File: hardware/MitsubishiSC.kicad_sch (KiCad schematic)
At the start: 68 parts, among them J1 CN105, J2 USB_C_Receptacle_USB2.0_16P, Q1 BSS138, Q2 BSS138, SW3 SPST, SW4 SPST, U1 TPS562203, U3 ESP32-C3-WROOM-02, U4 USBLC6-2SC6, U5 TLV75733PDBV

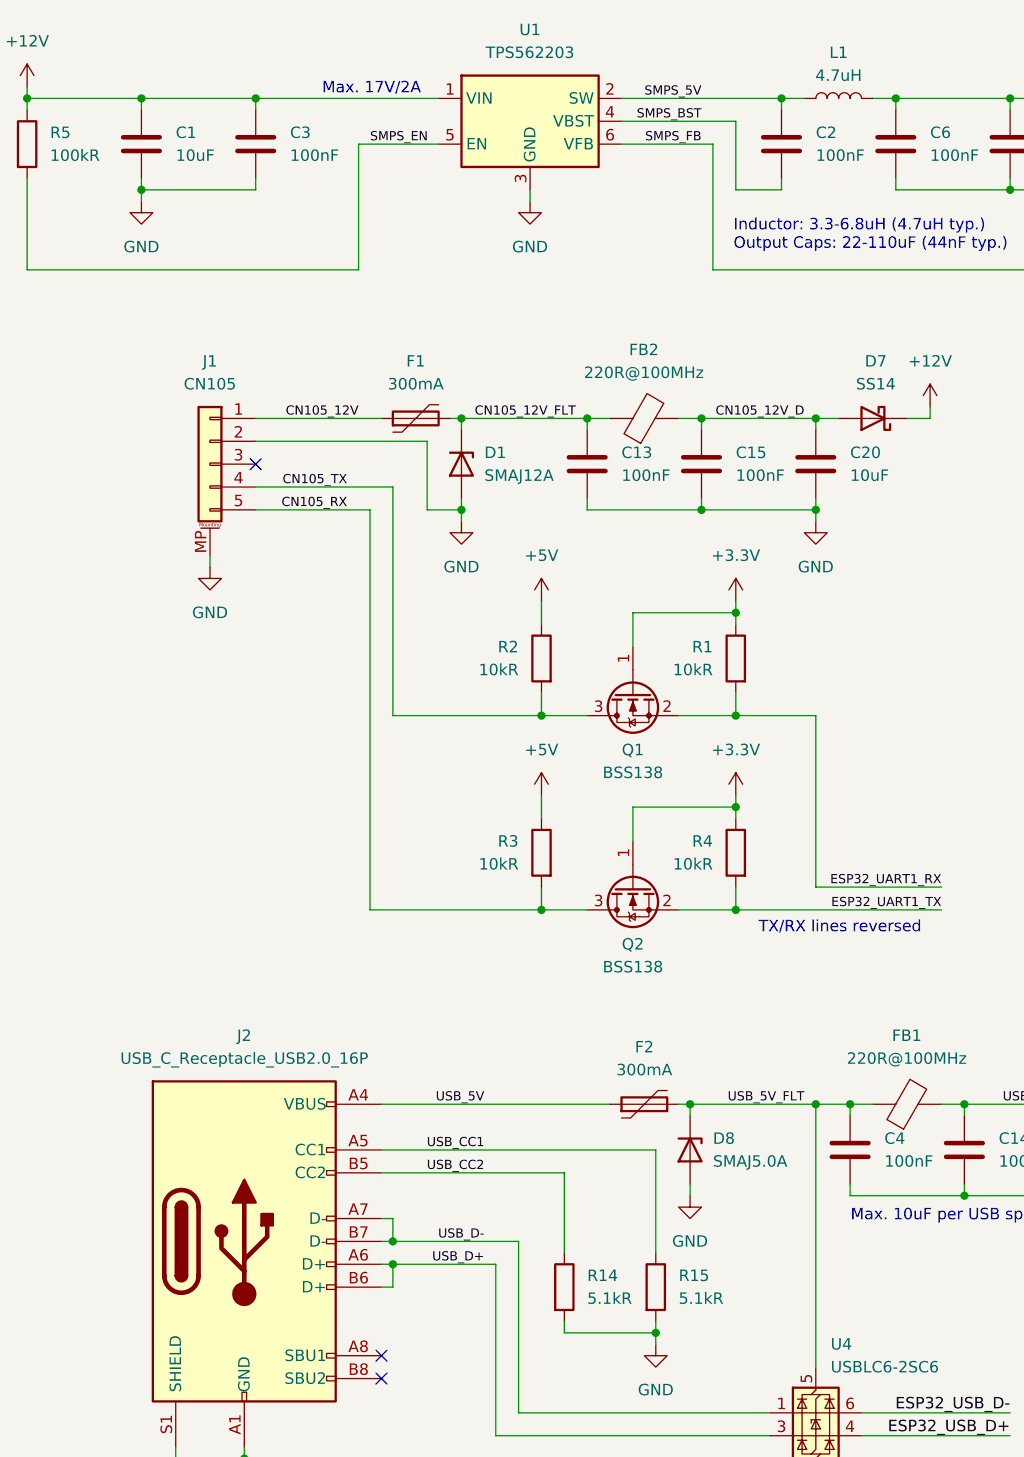
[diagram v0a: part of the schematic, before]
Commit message: feat: upgrade to KiCad v9 (#14)
This commit upgrades the KiCad files to `9.0.4`.
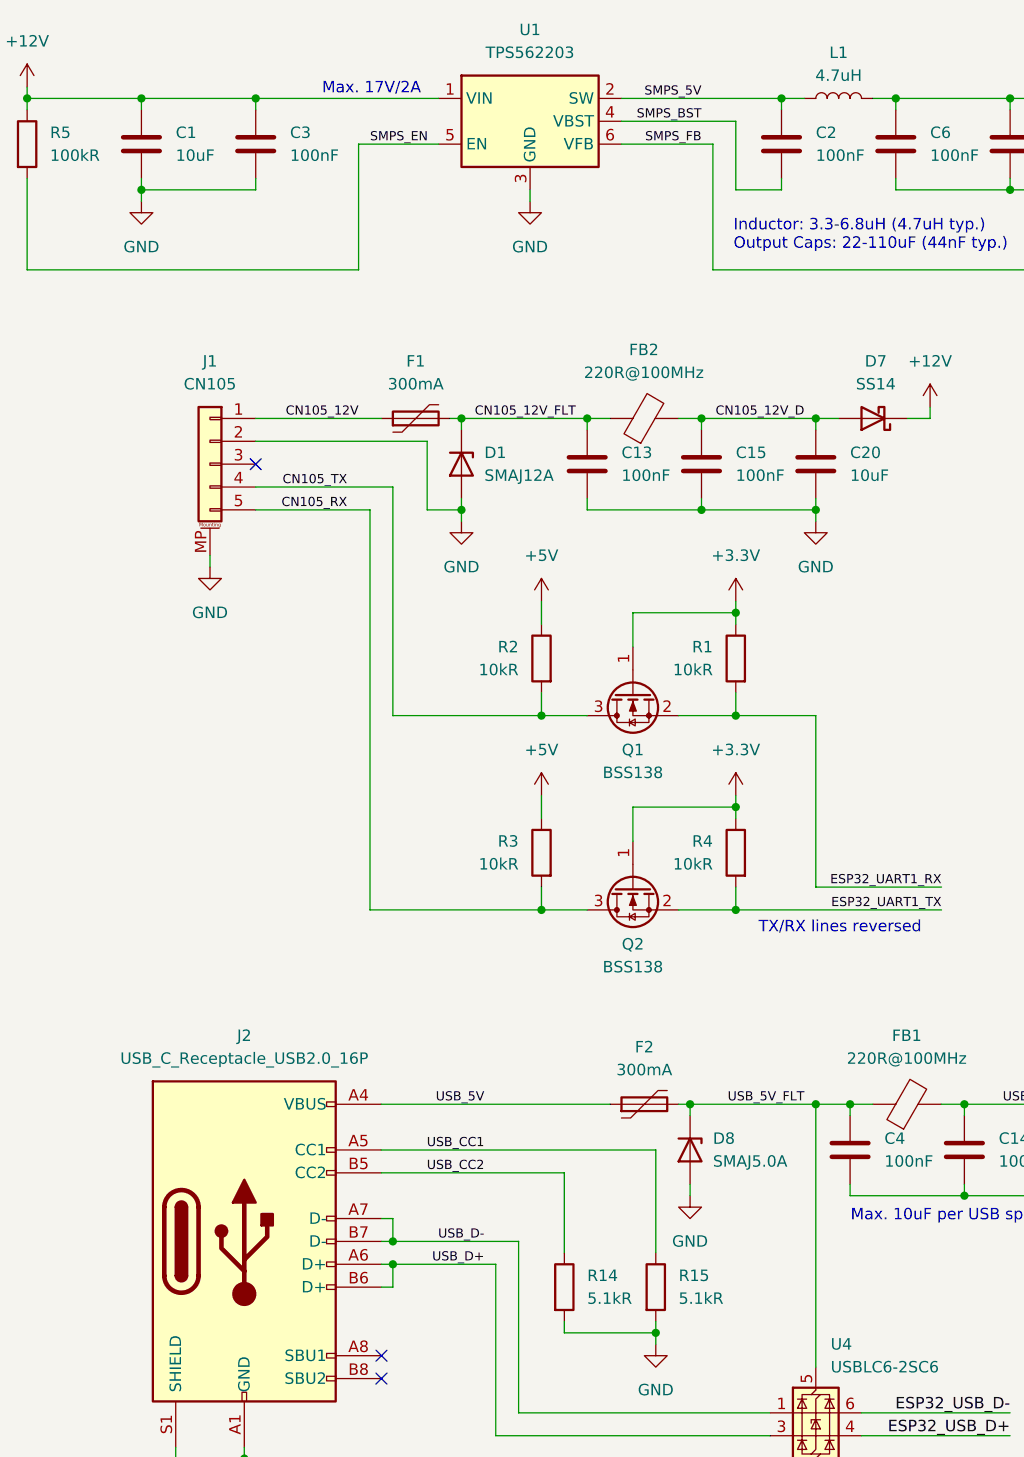
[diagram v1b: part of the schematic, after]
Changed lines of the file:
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@@
 (kicad_sch
-	(version 20231120)
+	(version 20250114)
 	(generator "eeschema")
-	(generator_version "8.0")
+	(generator_version "9.0")
 	(paper "A4")
 	(title_block
@@
 		(comment 1 "${BUILD_COMMIT}")
 	)
+	(text "TX/RX lines reversed"
+		(exclude_from_sim no)
+		(at 105.41 117.602 0)
+		(effects
+			(font
+				(size 1.27 1.27)
+			)
+			(justify left)
+		)
+	)
+	(text "Max. 17V/2A"
+		(exclude_from_sim no)
+		(at 56.896 24.384 0)
+		(effects
+			(font
+				(size 1.27 1.27)
+			)
+			(justify left)
+		)
+	)
+	(text "Inductor: 3.3-6.8uH (4.7uH typ.)\nOutput Caps: 22-110uF (44nF typ.)\n\n"
+		(exclude_from_sim no)
+		(at 102.616 41.656 0)
+		(effects
+			(font
+				(size 1.27 1.27)
+			)
+			(justify left)
+		)
+	)
+	(text "Max. 10uF per USB spec"
+		(exclude_from_sim no)
+		(at 126.238 149.606 0)
+		(effects
+			(font
+				(size 1.27 1.27)
+			)
+		)
+	)
+	(text "USB connector is used for flashing/debugging only"
+		(exclude_from_sim no)
+		(at 54.356 178.816 0)
+		(effects
+			(font
+				(size 1.27 1.27)
+			)
+			(justify left)
+		)
+	)
+	(text "Max. 5.5V/1A"
+		(exclude_from_sim no)
+		(at 217.678 23.368 0)
+		(effects
+			(font
+				(size 1.27 1.27)
+			)
+			(justify left)
+		)
+	)
+	(text "Resistors are thick film resistors rated for 75V ±1% or better, unless stated otherwise.\nCapacitors are Class II MLCCs rated for 25V ±10% 85°C or better, unless stated otherwise.\nFuses rated at 300mA have 30V rating and 600mA trip current."
+		(exclude_from_sim no)
+		(at 13.208 194.31 0)
+		(effects
+			(font
+				(size 1.27 1.27)
+			)
+			(justify left)
+		)
+	)
 	(junction
 		(at 115.57 137.16)
@@
 		)
 	)
-	(text "TX/RX lines reversed"
-		(exclude_from_sim no)
-		(at 105.41 117.602 0)
-		(effects
-			(font
-				(size 1.27 1.27)
-			)
-			(justify left)
-		)
-	)
-	(text "Max. 17V/2A"
-		(exclude_from_sim no)
-		(at 56.896 24.384 0)
-		(effects
-			(font
-				(size 1.27 1.27)
-			)
-			(justify left)
-		)
-	)
-	(text "Inductor: 3.3-6.8uH (4.7uH typ.)\nOutput Caps: 22-110uF (44nF typ.)\n\n"
-		(exclude_from_sim no)
-		(at 102.616 41.656 0)
-		(effects
-			(font
-				(size 1.27 1.27)
-			)
-			(justify left)
-		)
-	)
-	(text "Max. 10uF per USB spec"
-		(exclude_from_sim no)
-		(at 126.238 149.606 0)
-		(effects
-			(font
-				(size 1.27 1.27)
-			)
-		)
-	)
-	(text "USB connector is used for flashing/debugging only"
-		(exclude_from_sim no)
-		(at 54.356 178.816 0)
-		(effects
-			(font
-				(size 1.27 1.27)
-			)
-			(justify left)
-		)
-	)
-	(text "Max. 5.5V/1A"
-		(exclude_from_sim no)
-		(at 217.678 23.368 0)
-		(effects
-			(font
-				(size 1.27 1.27)
-			)
-			(justify left)
-		)
-	)
-	(text "Resistors are thick film resistors rated for 75V ±1% or better, unless stated otherwise.\nCapacitors are Class II MLCCs rated for 25V ±10% 85°C or better, unless stated otherwise.\nFuses rated at 300mA have 30V rating and 600mA trip current."
-		(exclude_from_sim no)
-		(at 13.208 194.31 0)
-		(effects
-			(font
-				(size 1.27 1.27)
-			)
-			(justify left)
-		)
-	)
 	(label "CN105_12V_D"
 		(at 110.49 60.96 180)
@@
 			)
 		)
-		(property "Datasheet" "https://www.lcsc.com/datasheet/lcsc_datasheet_2402181505_XINGLIGHT-XL-2012UBC_C965817.pdf"
+		(property "Datasheet" "~"
 			(at 200.66 130.81 0)
 			(effects
@@
 			)
 		)
+		(property "Sim.Pins" "1=K 2=A"
+			(at 200.66 130.81 0)
+			(effects
+				(font
+					(size 1.27 1.27)
+				)
+				(hide yes)
+			)
+		)
 		(pin "2"
 		)
@@
 			)
 		)
-		(property "Datasheet" "https://www.lcsc.com/datasheet/lcsc_datasheet_1811121616_onsemi-BSS138_C52895.pdf"
+		(property "Datasheet" "https://www.onsemi.com/pub/Collateral/BSS138-D.PDF"
 			(at 95.25 96.52 0)
 			(effects
@@
 			)
 		)
-		(property "Datasheet" "https://www.lcsc.com/datasheet/lcsc_datasheet_2402181505_XINGLIGHT-XL-2012SURC_C965812.pdf"
+		(property "Datasheet" "~"
 			(at 274.32 30.48 0)
 			(effects
@@
 			)
 		)
+		(property "Sim.Pins" "1=K 2=A"
+			(at 274.32 30.48 0)
+			(effects
+				(font
+					(size 1.27 1.27)
+				)
+				(hide yes)
+			)
+		)
 		(pin "2"
 		)
@@
 			)
 		)
-		(property "Datasheet" "https://www.lcsc.com/datasheet/lcsc_datasheet_1811121616_onsemi-BSS138_C52895.pdf"
+		(property "Datasheet" "https://www.onsemi.com/pub/Collateral/BSS138-D.PDF"
 			(at 95.25 118.11 0)
 			(effects
@@
 		)
 	)
+	(embedded_fonts no)
 )

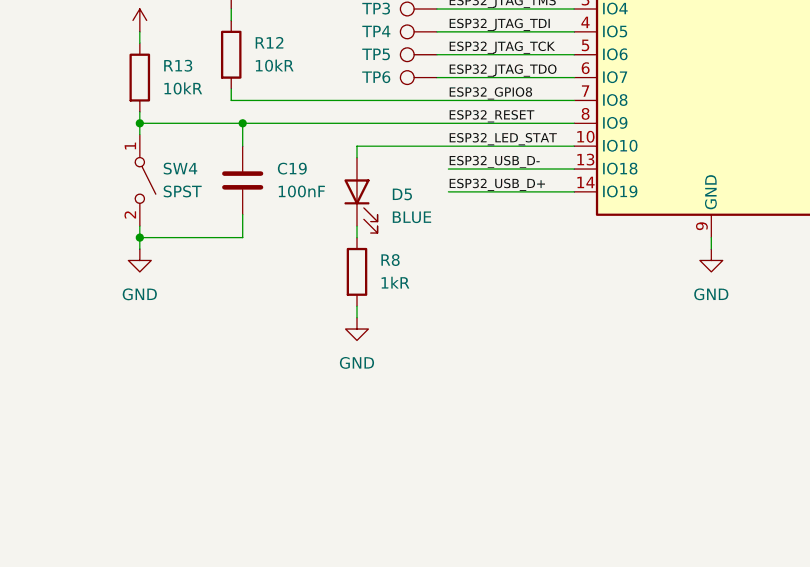
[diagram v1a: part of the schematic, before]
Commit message: feat(hw): reduce LED brightness
This commit reduces the brightness of the indicator LED by increasing
the resistor value of R8 from 1kR to 10kR. Although the resistor value
is on the higher side, this is generally fine because the use of LED is
not user-facing.
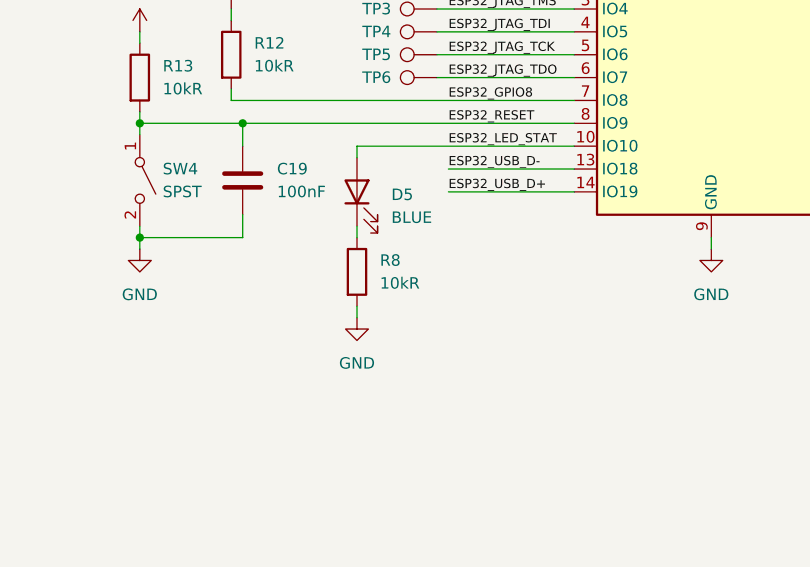
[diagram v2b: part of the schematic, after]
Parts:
- R8: value 1kR -> 10kR; Distributor Part Number C22548 -> C98220; Manufacturer Part Number RC0603FR-071KL -> RC0603FR-0710KL
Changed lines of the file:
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@@
 			)
 		)
-		(property "Value" "1kR"
+		(property "Value" "10kR"
 			(at 203.2 140.9699 0)
 			(effects
@@
 			)
 		)
-		(property "Datasheet" "https://www.lcsc.com/datasheet/lcsc_datasheet_2304140030_YAGEO-RC0603FR-071KL_C22548.pdf"
+		(property "Datasheet" "https://www.lcsc.com/datasheet/lcsc_datasheet_2304140030_YAGEO-RC0603FR-0710KL_C98220.pdf"
 			(at 200.66 139.7 0)
 			(effects
@@
 			)
 		)
-		(property "Distributor Part Number" "C22548"
+		(property "Distributor Part Number" "C98220"
 			(at 200.66 139.7 0)
 			(effects
@@
 			)
 		)
-		(property "Manufacturer Part Number" "RC0603FR-071KL"
+		(property "Manufacturer Part Number" "RC0603FR-0710KL"
 			(at 200.66 139.7 0)
 			(effects

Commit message: fix(hw): incorrect PPTC footprint
This commit fixes the incorrect PPTC footprint size.

The existing schematic specifies the Bourns MF-MSMF030-2 part which
should be using the `Fuse_1812_4532Metric` footprint but was instead
assigned the `Fuse_1206_3216Metric` footprint. As a result, the
component CANNOT be placed on the circuit board.

To rectify this, we changed the component to use the Littelfuse
1206L035/16 part instead, which is almost similar to the specifications
of the original part.

Importantly, a deliberate decision was made to swap component instead of
correcting the footprint in order to avoid the significant change to the
board layout required to accommodate the correct but larger 1812
footprint.
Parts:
- F1, F2: value 300mA -> 350mA; Distributor Part Number C12604 -> C126817; Manufacturer Bourns Inc. -> Littelfuse; Manufacturer Part Number MF-MSMF030-2 -> 1206L035/16
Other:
- note added: "Resistors are thick film resistors rated for 75V ±1% or better, unless stated otherwise. Capacitors are Class II MLCCs rated for 25V ±10% 85°C or better, unless stated otherwise. Fuses rated at 350mA have 16V rating and 750mA trip current."
- note removed: "Resistors are thick film resistors rated for 75V ±1% or better, unless stated otherwise. Capacitors are Class II MLCCs rated for 25V ±10% 85°C or better, unless stated otherwise. Fuses rated at 300mA have 30V rating and 600mA trip current."
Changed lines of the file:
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@@
 		)
 	)
-	(text "Resistors are thick film resistors rated for 75V ±1% or better, unless stated otherwise.\nCapacitors are Class II MLCCs rated for 25V ±10% 85°C or better, unless stated otherwise.\nFuses rated at 300mA have 30V rating and 600mA trip current."
+	(text "Resistors are thick film resistors rated for 75V ±1% or better, unless stated otherwise.\nCapacitors are Class II MLCCs rated for 25V ±10% 85°C or better, unless stated otherwise.\nFuses rated at 350mA have 16V rating and 750mA trip current."
 		(exclude_from_sim no)
 		(at 13.208 194.31 0)
@@
 			)
 		)
-		(property "Value" "300mA"
+		(property "Value" "350mA"
 			(at 67.31 57.15 90)
 			(effects
@@
 			)
 		)
-		(property "Datasheet" "https://www.lcsc.com/datasheet/lcsc_datasheet_1808271848_BOURNS-MF-MSMF030-2_C12604.pdf"
+		(property "Datasheet" "https://www.lcsc.com/datasheet/C126817.pdf"
 			(at 67.31 60.96 0)
 			(effects
@@
 			)
 		)
-		(property "Distributor Part Number" "C12604"
+		(property "Distributor Part Number" "C126817"
 			(at 67.31 60.96 0)
 			(effects
@@
 			)
 		)
-		(property "Manufacturer" "Bourns Inc."
+		(property "Manufacturer" "Littelfuse"
 			(at 67.31 60.96 0)
 			(effects
@@
 			)
 		)
-		(property "Manufacturer Part Number" "MF-MSMF030-2"
+		(property "Manufacturer Part Number" "1206L035/16"
 			(at 67.31 60.96 0)
 			(effects
@@
 			)
 		)
-		(property "Value" "300mA"
+		(property "Value" "350mA"
 			(at 92.71 133.35 90)
 			(effects
@@
 			)
 		)
-		(property "Datasheet" "https://www.lcsc.com/datasheet/lcsc_datasheet_1808271848_BOURNS-MF-MSMF030-2_C12604.pdf"
+		(property "Datasheet" "https://www.lcsc.com/datasheet/C126817.pdf"
 			(at 92.71 137.16 0)
 			(effects
@@
 			)
 		)
-		(property "Distributor Part Number" "C12604"
+		(property "Distributor Part Number" "C126817"
 			(at 92.71 137.16 0)
 			(effects
@@
 			)
 		)
-		(property "Manufacturer" "Bourns Inc."
+		(property "Manufacturer" "Littelfuse"
 			(at 92.71 137.16 0)
 			(effects
@@
 			)
 		)
-		(property "Manufacturer Part Number" "MF-MSMF030-2"
+		(property "Manufacturer Part Number" "1206L035/16"
 			(at 92.71 137.16 0)
 			(effects
